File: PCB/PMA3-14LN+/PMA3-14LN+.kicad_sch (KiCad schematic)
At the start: 19 parts, among them J1 Conn_Coaxial, J2 Conn_Coaxial, U1 PMA3-14LN+, U2 L7806

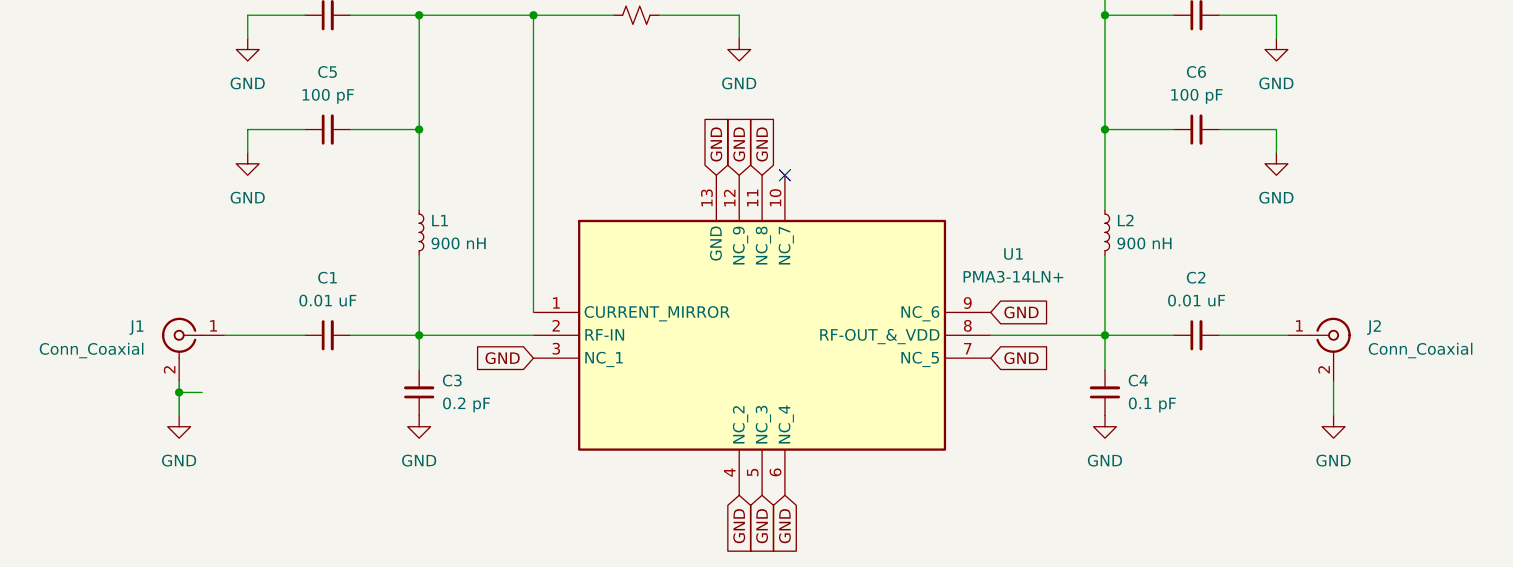
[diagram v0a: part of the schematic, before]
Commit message: Rev C PMA3-14LN+ - Pad Size Change
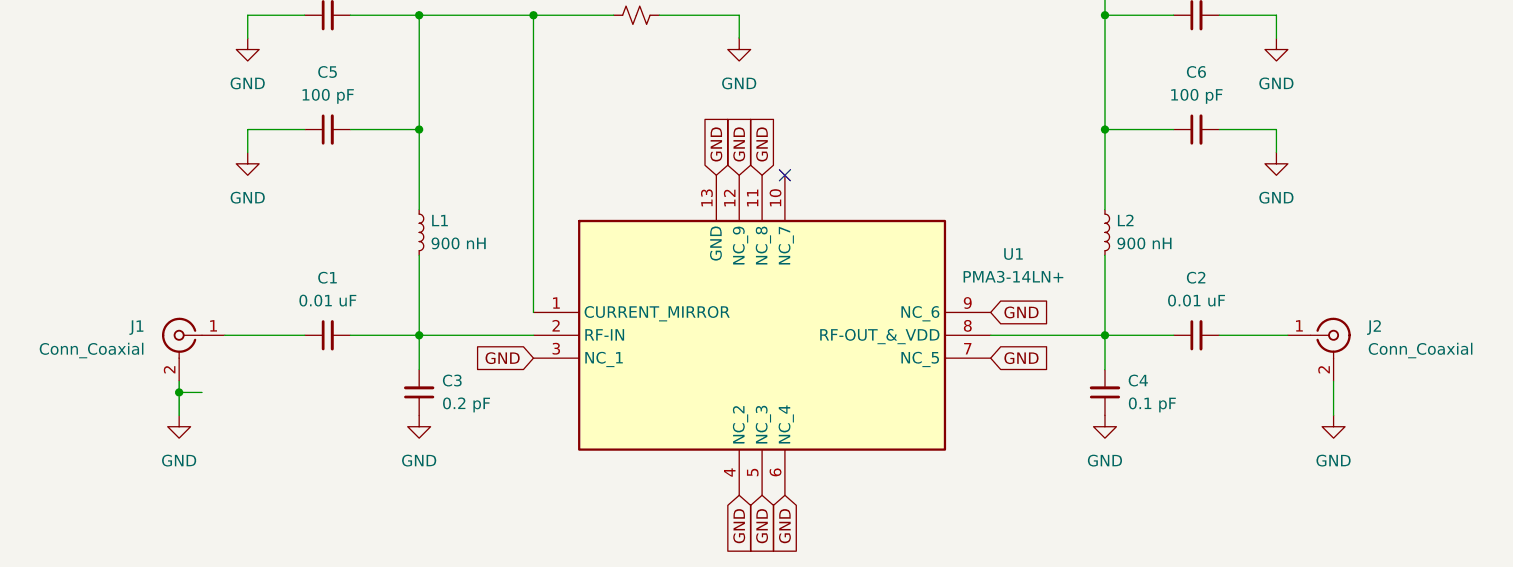
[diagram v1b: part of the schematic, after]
